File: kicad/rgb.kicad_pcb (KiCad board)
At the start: 2 copper layers, 3 parts, among them Q1 PMV15ENEA, Q2 PMV15ENEA, U1 ATTINY404-SSNR

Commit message: Starting schematics
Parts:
- added Q3: IRLML6244, rgb_footprints:SOT23_HandSoldering_mini, F.Cu at (194.0, 97.0)
- added Q4: IRLML6244, rgb_footprints:SOT23_HandSoldering_mini, F.Cu at (199.0, 97.0)
- added Q5: IRLML6244, rgb_footprints:SOT23_HandSoldering_mini, F.Cu at (183.8, 101.2)
- added Q6: IRLML6244, rgb_footprints:SOT23_HandSoldering_mini, F.Cu at (188.8, 101.0)
- added Q7: IRLML6244, rgb_footprints:SOT23_HandSoldering_mini, F.Cu at (194.0, 101.0)
- added Q8: IRLML6244, rgb_footprints:SOT23_HandSoldering_mini, F.Cu at (199.0, 101.0)
- Q1, Q2: value PMV15ENEA -> IRLML6244; footprint Package_TO_SOT_SMD:SOT-23_Handsoldering -> rgb_footprints:SOT23_HandSoldering_mini
- U1: value ATTINY404-SSNR -> ATTINY404
- moved Q1 78.0 mm to (183.8, 97.0), turned to 90 degrees
- moved Q2 76.2 mm to (188.8, 97.0), turned to 90 degrees
- moved U1 42.4 mm to (207.0, 99.0)

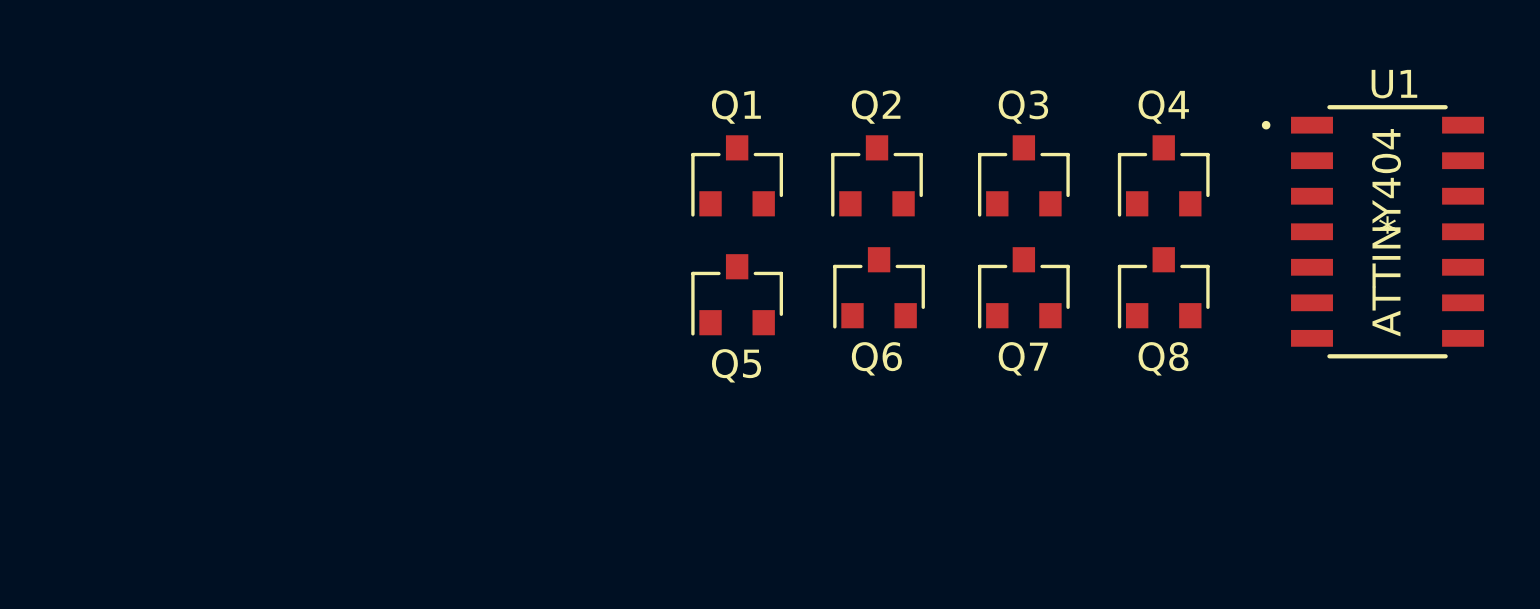
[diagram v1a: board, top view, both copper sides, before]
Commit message: changed mosfets
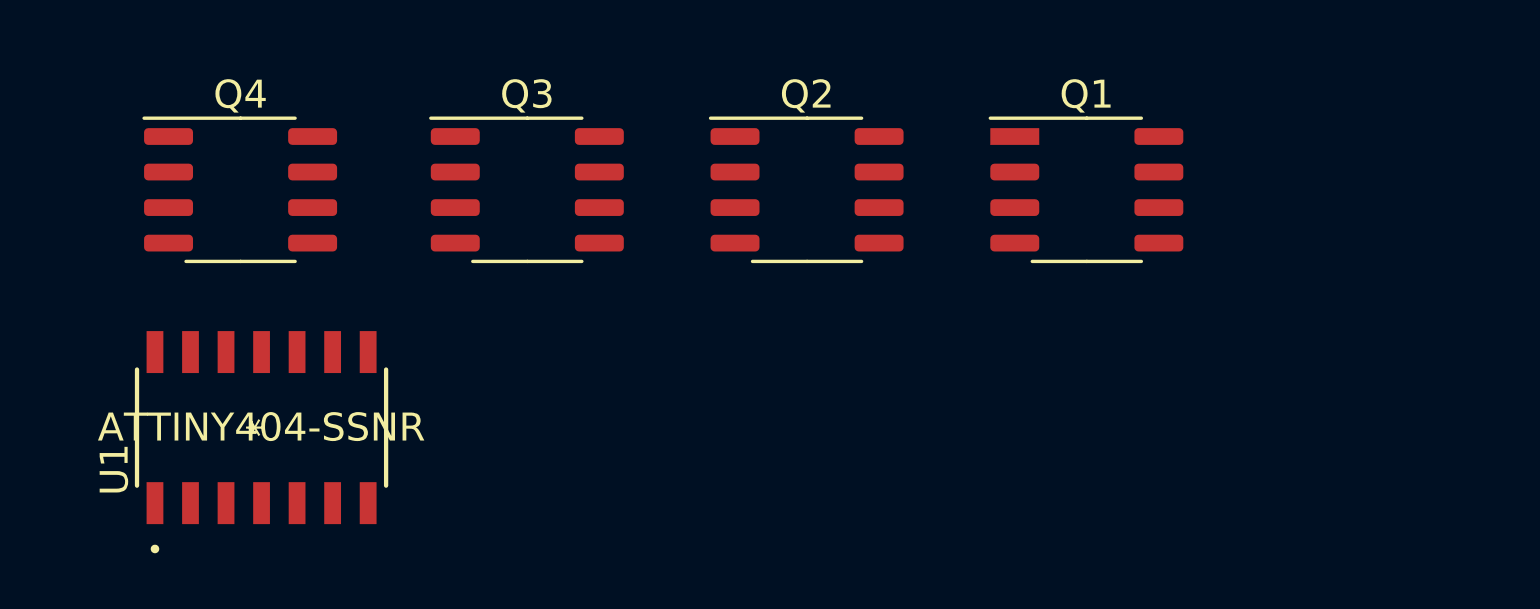
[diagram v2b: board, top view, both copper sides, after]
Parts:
- removed Q5, Q6, Q7, Q8: IRLML6244, rgb_footprints:SOT23_HandSoldering_mini
- Q1, Q2, Q3, Q4: value IRLML6244 -> DMG9926USD; footprint rgb_footprints:SOT23_HandSoldering_mini -> Package_SO:SO-8_3.9x4.9mm_P1.27mm
- U1: value ATTINY404 -> ATTINY404-SSNR
- moved U1 40.9 mm to (166.8, 106.0), turned to 90 degrees
- moved Q4 33.0 mm to (166.0, 97.5), turned to 0 degrees
- moved Q3 17.8 mm to (176.2, 97.5), turned to 0 degrees
- moved Q1 12.5 mm to (196.2, 97.5), turned to 0 degrees
- moved Q2 2.55 mm to (186.2, 97.5), turned to 0 degrees
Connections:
- Q1 pad 2: GND -> (no net)
- Q2 pad 2: GND -> (no net)
- Q3 pad 2: GND -> (no net)
- Q4 pad 2: GND -> (no net)

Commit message: ATTINY216
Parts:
- U1: value ATTINY404-SSNR -> ATtiny416-SNR; footprint rgb_footprints:ATTINY404-SSNR -> Package_SO:SOIC-20W_7.5x12.8mm_P1.27mm
- moved U1 22.8 mm to (171.8, 83.8), turned to 0 degrees
- moved Q2 16.0 mm to (170.2, 98.2)
- moved Q4 12.7 mm to (178.7, 98.2)
- moved Q3 9.37 mm to (170.2, 104.7)
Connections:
- Q1 pad 1: (no net) -> GND
- Q1 pad 2: (no net) -> /PWM_1
- Q1 pad 3: (no net) -> GND
- Q1 pad 4: (no net) -> /PWM_2
- Q2 pad 1: (no net) -> GND
- Q2 pad 2: (no net) -> /PWM_3
- Q2 pad 3: (no net) -> GND
- Q2 pad 4: (no net) -> /PWM_4
- Q3 pad 1: (no net) -> GND
- Q3 pad 3: (no net) -> GND
- Q4 pad 1: (no net) -> GND
- Q4 pad 2: (no net) -> /PWM_7
- Q4 pad 3: (no net) -> GND
- Q4 pad 4: (no net) -> /PWM_8
- U1 pad 10: (no net) -> /PWM_2
- U1 pad 11: (no net) -> /PWM_1
- U1 pad 12: (no net) -> /PWM_7
- U1 pad 13: (no net) -> /PWM_8
- U1 pad 9: (no net) -> /PWM_3

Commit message: Schematics work
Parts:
- added F1: 0685H9200-01, Fuse:Fuse_1206_3216Metric_Pad1.42x1.75mm_HandSolder, F.Cu at (183.8, 99.2)
- added F2: 0679L9100-01, Fuse:Fuse_1206_3216Metric_Pad1.42x1.75mm_HandSolder, F.Cu at (183.8, 104.0)
- added F3: 0679L9100-01, Fuse:Fuse_1206_3216Metric_Pad1.42x1.75mm_HandSolder, F.Cu at (183.5, 109.0)
- added SW1: 1825232-1, rgb_footprints:Switch_Slide_1825232-1, F.Cu at (137.8, 92.0)
- added U2: AP63205WU-7, rgb_footprints:AP63205WU-7, F.Cu at (138.0, 84.5)
- Q1, Q2, Q3, Q4: footprint Package_SO:SO-8_3.9x4.9mm_P1.27mm -> rgb_footprints:DMG9926USD_Handsolder
- U1: footprint Package_SO:SOIC-20W_7.5x12.8mm_P1.27mm -> rgb_footprints:ATTINY416-SNR
- moved Q1 49.8 mm to (146.8, 103.2)
- moved U1 20.8 mm to (151.5, 88.5)
- moved Q2 15.8 mm to (155.2, 103.2)
- moved Q4 8.16 mm to (172.2, 103.2)
- moved Q3 6.66 mm to (163.8, 103.2)
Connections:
- Q3 pad 2: (no net) -> /PWM_5
- Q3 pad 4: (no net) -> /PWM_6
- U1 pad 1: (no net) -> +5V
- U1 pad 2: (no net) -> /PWM_5
- U1 pad 3: (no net) -> /PWM_6

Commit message: Connectors / protection
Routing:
- net +12V: track 0.00 -> 5.68 mm

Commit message: footprints
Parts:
- added C1: 10 uF, Capacitor_SMD:C_0805_2012Metric_Pad1.18x1.45mm_HandSolder, F.Cu at (119.4, 85.1)
- added C2: 100 nF, Capacitor_SMD:C_0603_1608Metric_Pad1.08x0.95mm_HandSolder, F.Cu at (118.7, 88.6)
- added C3: 22 uF, Capacitor_SMD:C_0805_2012Metric_Pad1.18x1.45mm_HandSolder, F.Cu at (114.1, 88.8)
- added C4: 22 uF, Capacitor_SMD:C_0805_2012Metric_Pad1.18x1.45mm_HandSolder, F.Cu at (135.2, 76.5)
- added C5: 100 nF, Capacitor_SMD:C_0603_1608Metric_Pad1.08x0.95mm_HandSolder, F.Cu at (118.1, 71.1)
- added D1: LED, LED_SMD:LED_0805_2012Metric_Pad1.15x1.40mm_HandSolder, F.Cu at (118.4, 68.3)
- added F1: 0685H9200-01, Fuse:Fuse_1206_3216Metric_Pad1.42x1.75mm_HandSolder, F.Cu at (166.3, 72.3)
- added J1: 1935776, rgb_footprints:barrel jack, F.Cu at (144.8, 69.8)
- added J2: Conn_01x05, rgb_footprints:CUI_TB003-500-P05BE, F.Cu at (174.0, 80.0)
- added J3: Conn_01x05, rgb_footprints:CUI_TB003-500-P05BE, F.Cu at (174.0, 90.3)
- added J4: Conn_01x04, Connector_PinHeader_2.54mm:PinHeader_1x03_P2.54mm_Vertical, F.Cu at (130.8, 63.5)
- added J5: Conn_01x02, Connector_PinHeader_2.54mm:PinHeader_1x04_P2.54mm_Vertical, F.Cu at (126.2, 63.5)
- added L1: 4.7 uH, Inductor_SMD:L_1008_2520Metric_Pad1.43x2.20mm_HandSolder, F.Cu at (114.3, 85.5)
- added R1: 15 kΩ, Resistor_SMD:R_0603_1608Metric_Pad0.98x0.95mm_HandSolder, F.Cu at (124.0, 84.8)
- added R2: 10 kΩ, Resistor_SMD:R_0603_1608Metric_Pad0.98x0.95mm_HandSolder, F.Cu at (135.0, 79.3)
- added R3: 1 kΩ, Resistor_SMD:R_0603_1608Metric_Pad0.98x0.95mm_HandSolder, F.Cu at (128.3, 84.8)
- added SW1: SW_Push, Button_Switch_THT:SW_PUSH_6mm_H13mm, F.Cu at (113.7, 77.1)
- added SW2: Rotary_Encoder, rgb_footprints:rotary encoder, F.Cu at (170.2, 40.6)
- added SW3: Rotary_Encoder, rgb_footprints:rotary encoder, F.Cu at (170.2, 57.3)
- added SW4: Rotary_Encoder, rgb_footprints:rotary encoder, F.Cu at (185.4, 40.6)
- added SW5: Rotary_Encoder, rgb_footprints:rotary encoder, F.Cu at (200.7, 40.6)
- added SW6: SW_Push, Button_Switch_THT:SW_PUSH_6mm_H13mm, F.Cu at (124.3, 77.1)
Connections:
- Q1 pad 6: (no net) -> /DRAIN_2
- Q1 pad 8: (no net) -> /DRAIN_1
- Q2 pad 6: (no net) -> /DRAIN_4
- Q2 pad 8: (no net) -> /DRAIN_3
- Q3 pad 6: (no net) -> /DRAIN_6
- Q3 pad 8: (no net) -> /DRAIN_5
- Q4 pad 6: (no net) -> /DRAIN_8
- Q4 pad 8: (no net) -> /DRAIN_7
- U1 pad 14: (no net) -> /SW2_A
- U1 pad 15: (no net) -> /SW3_A
- U1 pad 16: (no net) -> /RESET
- U1 pad 17: (no net) -> /TWI_SDA
- U1 pad 18: (no net) -> /TWI_SCL
- U1 pad 4: (no net) -> /SW4_A
- U1 pad 5: (no net) -> /SW5_A
- U1 pad 6: (no net) -> /PWR_EN
- U1 pad 7: (no net) -> /SW6
- U1 pad 8: (no net) -> /SW_B
- U2 pad 2: Net-(SW1-Pad2) -> /PWR_EN
- U2 pad 5: (no net) -> Net-(C2-Pad2)
- U2 pad 6: (no net) -> Net-(C2-Pad1)
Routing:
- net +12V: track 5.68 -> 0.00 mm

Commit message: bulk capacitor
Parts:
- removed C2: 100 nF, Capacitor_SMD:C_0603_1608Metric_Pad1.08x0.95mm_HandSolder
- removed the C4 at (135.2, 76.5)
- removed the F1 at (183.8, 99.2)
- removed F2, F3: 0679L9100-01, Fuse:Fuse_1206_3216Metric_Pad1.42x1.75mm_HandSolder
- removed L1: 4.7 uH, Inductor_SMD:L_1008_2520Metric_Pad1.43x2.20mm_HandSolder
- removed the SW1 at (137.8, 92.0)
- C1: value 10 uF -> 220 uF; footprint Capacitor_SMD:C_0805_2012Metric_Pad1.18x1.45mm_HandSolder -> Capacitor_SMD:CP_Elec_6.3x7.7
- C3: value 22 uF -> 470 nF; footprint Capacitor_SMD:C_0805_2012Metric_Pad1.18x1.45mm_HandSolder -> Capacitor_SMD:C_0805_2012Metric_Pad1.15x1.40mm_HandSolder
- R1: value 15 kΩ -> 100k; footprint Resistor_SMD:R_0603_1608Metric_Pad0.98x0.95mm_HandSolder -> Resistor_SMD:R_0603_1608Metric_Pad1.05x0.95mm_HandSolder
- R2: value 10 kΩ -> 50k; footprint Resistor_SMD:R_0603_1608Metric_Pad0.98x0.95mm_HandSolder -> Resistor_SMD:R_0603_1608Metric_Pad1.05x0.95mm_HandSolder
- U2: value AP63205WU-7 -> MIC5203; footprint rgb_footprints:AP63205WU-7 -> digikey-footprints:SOT-143-4
- moved SW3 60.0 mm to (230.0, 61.2)
- moved C1 54.4 mm to (169.0, 62.8), turned to 180 degrees
- moved J2 54.3 mm to (228.2, 83.0)
- moved J3 54.3 mm to (228.2, 93.3)
- moved R2 46.3 mm to (94.2, 101.2)
- moved U2 44.4 mm to (94.3, 92.8)
- moved D1 33.0 mm to (99.2, 95.2)
- moved R1 32.9 mm to (94.2, 98.7)
- moved C4 28.9 mm to (146.2, 77.8)
- moved SW2 25.3 mm to (184.9, 61.1)
- moved SW4 25.3 mm to (200.2, 61.1)
- moved SW5 25.3 mm to (215.4, 61.1)
- moved C3 15.4 mm to (99.0, 91.8)
- moved F1 15.2 mm to (152.5, 66.0)
- moved J1 7.07 mm to (148.8, 64.0)
- renumbered C5 to C4
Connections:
- C1 pad 1: GND -> +12V
- C1 pad 2: +12V -> GND
- R1 pad 1: Net-(R1-Pad1) -> /PWR_EN
- R1 pad 2: /PWR_EN -> Net-(R1-Pad2)
- SW1 pad 2: Net-(R1-Pad1) -> Net-(R1-Pad2)
- U2 pad 1: +5V -> GND
- U2 pad 4: GND -> +5V

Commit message: layout start
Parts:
- C1, C3, C4, D1, F1, Q1, Q2, Q3, Q4, R1, R2, R3, U1, U2: moved to B.Cu
- moved SW3 183.7 mm to (48.0, 86.3)
- moved SW5 183.7 mm to (33.4, 86.3)
- moved J2 170.4 mm to (58.2, 95.4)
- moved J3 161.1 mm to (69.0, 68.3)
- moved SW4 152.4 mm to (48.0, 70.3)
- moved SW2 151.8 mm to (33.4, 70.3)
- moved J4 109.2 mm to (27.7, 99.5), turned to 90 degrees
- moved U1 104.3 mm to (47.6, 79.3), turned to 90 degrees
- moved J5 94.8 mm to (38.5, 99.5), turned to 90 degrees
- moved Q3 92.5 mm to (76.1, 73.8), turned to 90 degrees
- moved Q4 91.2 mm to (85.9, 73.8), turned to 90 degrees
- moved Q1 81.9 mm to (66.0, 90.0), turned to 270 degrees
- moved Q2 80.6 mm to (75.8, 90.1), turned to 270 degrees
- moved C1 68.7 mm to (102.8, 81.3), turned to 0 degrees
- moved SW6 67.1 mm to (57.3, 73.1)
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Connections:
- Q3 pad 2: /PWM_5 -> /PWM_6
- Q3 pad 4: /PWM_6 -> /PWM_5
- Q3 pad 6: /DRAIN_6 -> /DRAIN_5
- Q3 pad 8: /DRAIN_5 -> /DRAIN_6
- Q4 pad 2: /PWM_7 -> /PWM_8
- Q4 pad 4: /PWM_8 -> /PWM_7
- Q4 pad 6: /DRAIN_8 -> /DRAIN_7
- Q4 pad 8: /DRAIN_7 -> /DRAIN_8
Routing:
- added copper zone on B.Cu, net /DRAIN_1
